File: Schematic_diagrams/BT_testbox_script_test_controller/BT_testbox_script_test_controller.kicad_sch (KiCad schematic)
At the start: 28 parts, among them J10 Conn_01x15_Socket, J3 D Sub Conn_15_Pin Female, J4 Conn_01x07_Socket, J5 Conn_7_Pin, SW4 SW_Push

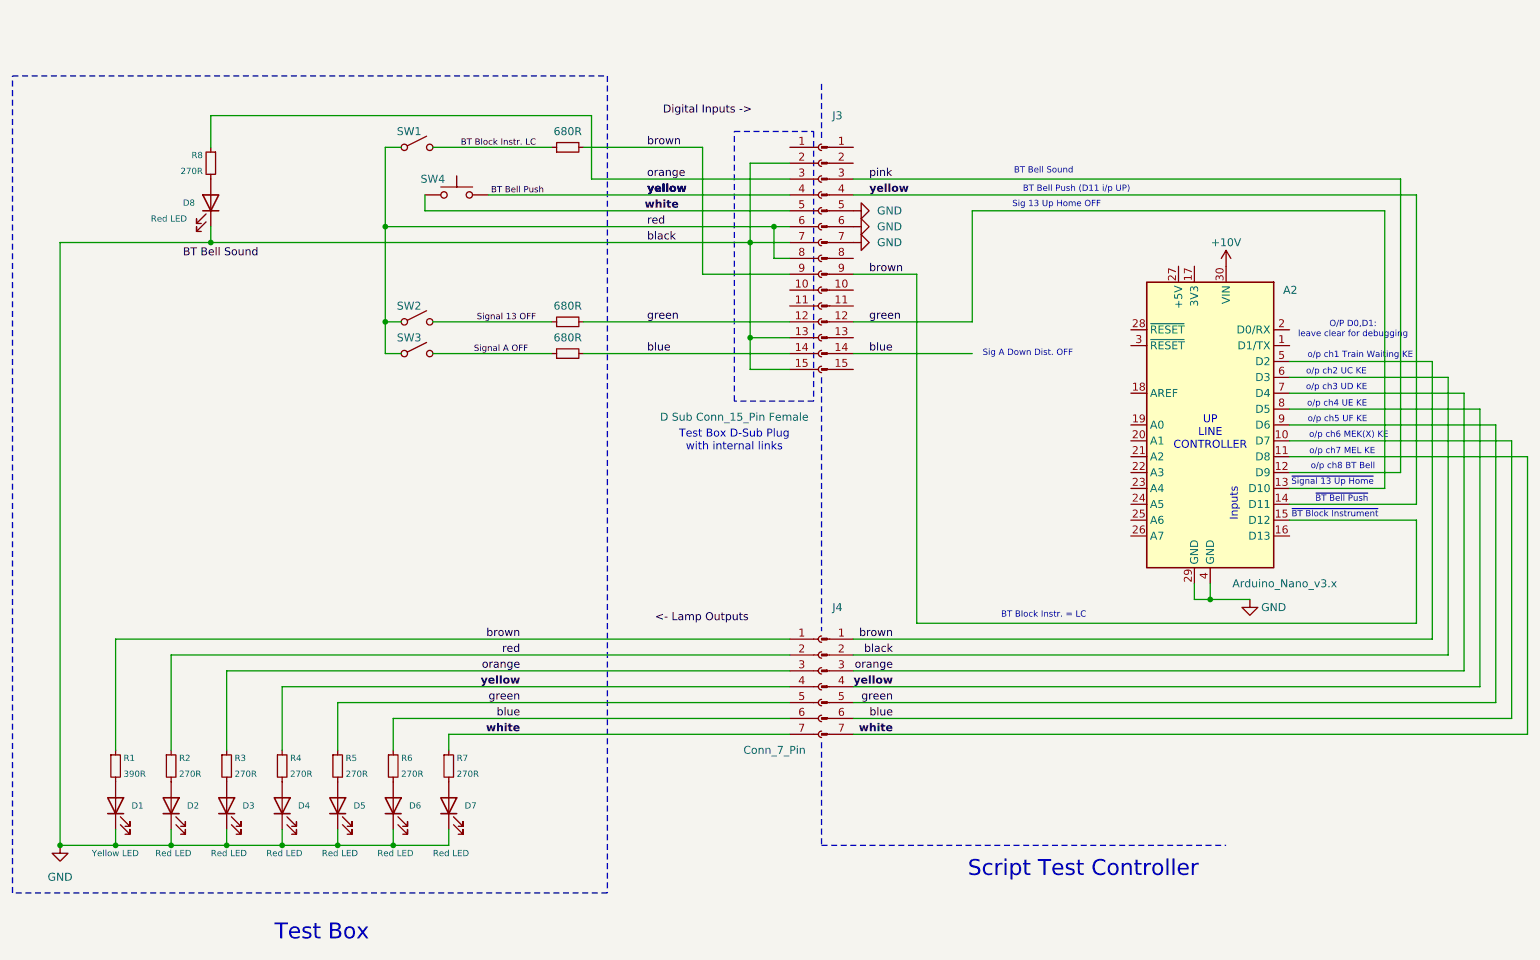
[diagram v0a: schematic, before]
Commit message: internal signal trial
trial was abandoned (inconsistent operation of interrupt)
though some changes were made to wiring and delays
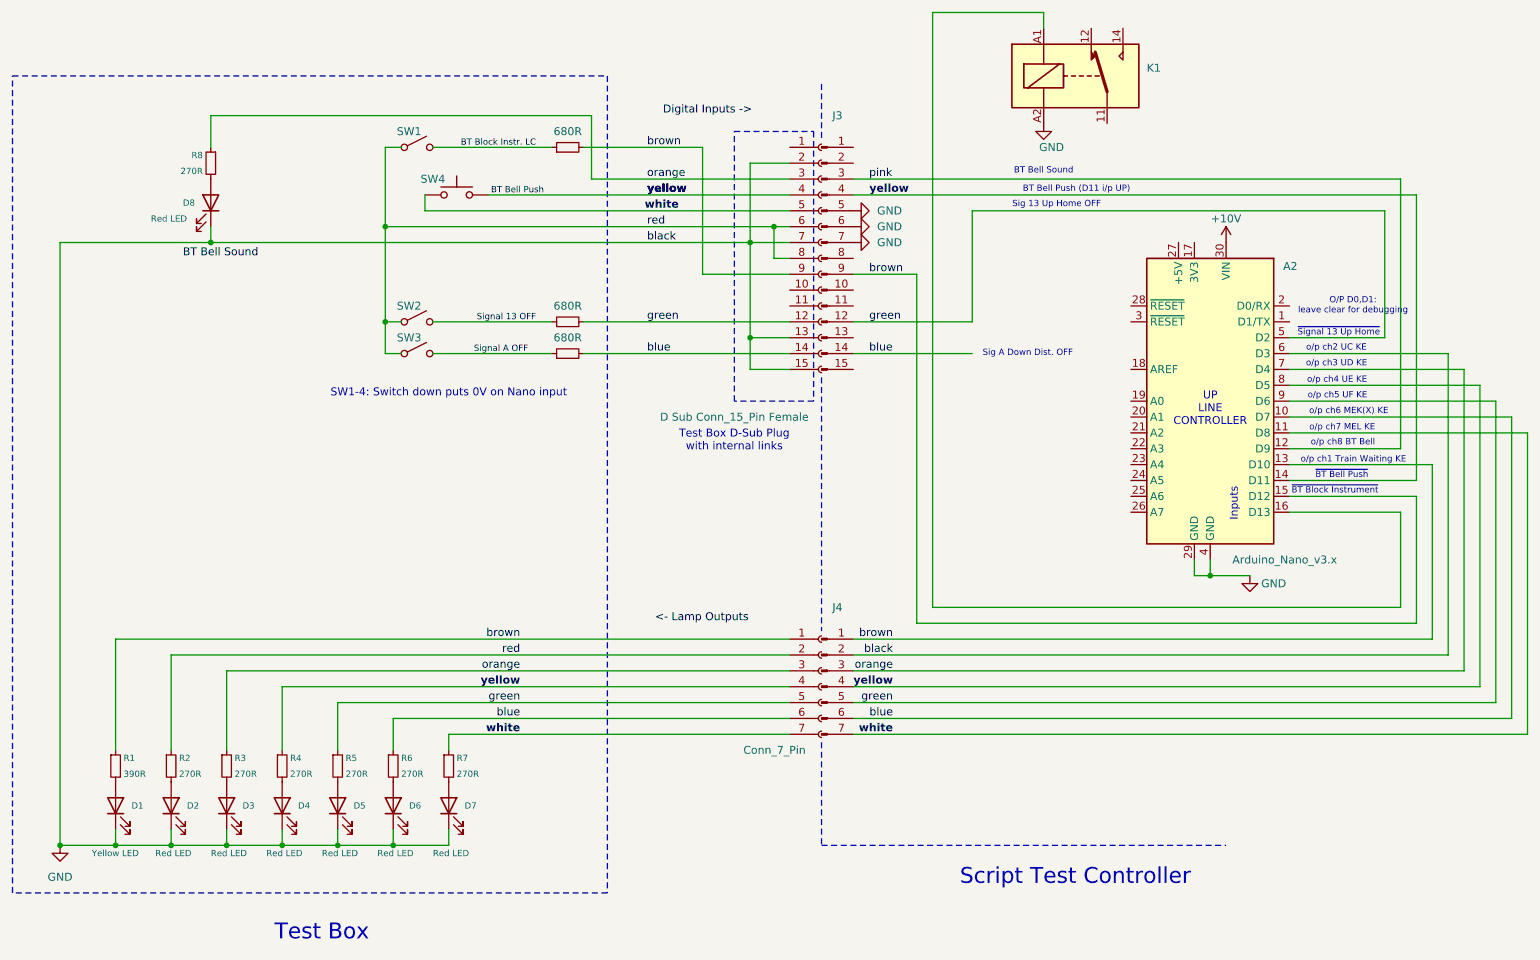
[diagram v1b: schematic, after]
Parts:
- added K1: ~, Relay_THT:Relay_SPDT_Fujitsu_FTR-LYCA005x_FormC_Vertical, symbol Relay:Fujitsu_FTR-LYCA005x
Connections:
- net GND: now also K1.A2
- net brown: now also A2.13 (D10); no longer A2.5 (D2)
- net green: now also A2.5 (D2); no longer A2.13 (D10)
- net at A2.16 (D13): now also K1.A1
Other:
- note added: "SW1-4: Switch down puts 0V on Nano input"
- note removed: "BT Block Instr. = LC"
- moved on the sheet: A2

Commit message: Jim request
train held at second lamp until distant reversed
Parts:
- removed K1: ~, Relay_THT:Relay_SPDT_Fujitsu_FTR-LYCA005x_FormC_Vertical, symbol Relay:Fujitsu_FTR-LYCA005x
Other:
- note added: "Sig A Down Dist. OFF (DOWN line test, connect to D9)"
- note removed: "Sig A Down Dist. OFF"
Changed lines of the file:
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@@
 		(company "Amberley Museum")
 		(comment 1 "B: model signal added")
+		(comment 2 "C: model signal removed; wiring shown for UP line test")
 	)
 	(rectangle
@@
 		)
 	)
-	(text "Sig A Down Dist. OFF"
+	(text "Sig A Down Dist. OFF\n(DOWN line test, connect to D9)"
 		(exclude_from_sim no)
-		(at 200.66 72.39 0)
+		(at 200.66 73.66 0)
 		(effects
 			(font
@@
 	(wire
 		(pts
-			(xy 185.42 17.78) (xy 185.42 113.03)
-		)
-		(stroke
-			(width 0)
-			(type default)
-		)
-	)
-	(wire
-		(pts
 			(xy 162.56 54.61) (xy 156.21 54.61)
 		)
@@
 	(wire
 		(pts
-			(xy 260.35 97.79) (xy 242.57 97.79)
-		)
-		(stroke
-			(width 0)
-			(type default)
-		)
-	)
-	(wire
-		(pts
 			(xy 172.72 133.35) (xy 280.67 133.35)
 		)
@@
 	(wire
 		(pts
-			(xy 203.2 20.32) (xy 203.2 17.78)
-		)
-		(stroke
-			(width 0)
-			(type default)
-		)
-	)
-	(wire
-		(pts
 			(xy 107.95 133.35) (xy 162.56 133.35)
 		)
@@
 	(wire
 		(pts
-			(xy 260.35 113.03) (xy 260.35 97.79)
-		)
-		(stroke
-			(width 0)
-			(type default)
-		)
-	)
-	(wire
-		(pts
 			(xy 156.21 41.91) (xy 156.21 54.61)
 		)
@@
 	(wire
 		(pts
-			(xy 185.42 113.03) (xy 260.35 113.03)
-		)
-		(stroke
-			(width 0)
-			(type default)
-		)
-	)
-	(wire
-		(pts
 			(xy 130.81 34.29) (xy 69.85 34.29)
 		)
@@
 	(wire
 		(pts
-			(xy 203.2 17.78) (xy 185.42 17.78)
-		)
-		(stroke
-			(width 0)
-			(type default)
-		)
-	)
-	(wire
-		(pts
 			(xy 227.33 105.41) (xy 227.33 107.95)
 		)
@@
 	)
 	(symbol
-		(lib_id "power:GND")
-		(at 203.2 35.56 0)
-		(unit 1)
-		(exclude_from_sim no)
-		(in_bom yes)
-		(on_board yes)
-		(dnp no)
-		(property "Reference" "#PWR04"
-			(at 203.2 41.91 0)
-			(effects
-				(font
-					(size 1.27 1.27)
-				)
-				(hide yes)
-			)
-		)
-		(property "Value" "GND"
-			(at 204.47 39.37 0)
-			(effects
-				(font
-					(size 1.27 1.27)
-				)
-			)
-		)
-		(property "Footprint" ""
-			(at 203.2 35.56 0)
-			(effects
-				(font
-					(size 1.27 1.27)
-				)
-				(hide yes)
-			)
-		)
-		(property "Datasheet" ""
-			(at 203.2 35.56 0)
-			(effects
-				(font
-					(size 1.27 1.27)
-				)
-				(hide yes)
-			)
-		)
-		(property "Description" "Power symbol creates a global label with name \"GND\" , ground"
-			(at 203.2 35.56 0)
-			(effects
-				(font
-					(size 1.27 1.27)
-				)
-				(hide yes)
-			)
-		)
-		(pin "1"
-		)
-		(instances
-			(project ""
-				(path "/aad29df0-d981-468f-91fb-fd321cbc3a70"
-					(reference "#PWR04")
-					(unit 1)
-				)
-			)
-		)
-	)
-	(symbol
 		(lib_id "Device:LED")
 		(at 69.85 48.26 270)
@@
 					(unit 1)
 				)
-			)
-		)
-	)
-	(symbol
-		(lib_id "Relay:Fujitsu_FTR-LYCA005x")
-		(at 208.28 27.94 0)
-		(unit 1)
-		(exclude_from_sim no)
-		(in_bom yes)
-		(on_board yes)
-		(dnp no)
-		(fields_autoplaced yes)
-		(property "Reference" "K1"
-			(at 219.71 26.6699 0)
-			(effects
-				(font
-					(size 1.27 1.27)
-				)
-				(justify left)
-			)
-		)
-		(property "Value" "~"
-			(at 219.71 29.2099 0)
-			(effects
-				(font
-					(size 1.27 1.27)
-				)
-				(justify left)
-			)
-		)
-		(property "Footprint" "Relay_THT:Relay_SPDT_Fujitsu_FTR-LYCA005x_FormC_Vertical"
-			(at 219.71 29.21 0)
-			(effects
-				(font
-					(size 1.27 1.27)
-				)
-				(justify left)
-				(hide yes)
-			)
-		)
-		(property "Datasheet" "https://www.fujitsu.com/sg/imagesgig5/ftr-ly.pdf"
-			(at 224.79 31.75 0)
-			(effects
-				(font
-					(size 1.27 1.27)
-				)
-				(justify left)
-				(hide yes)
-			)
-		)
-		(property "Description" "Relay, SPDT Form C, vertical mount, 5-60V coil, 6A, 250VAC, 28 x 5 x 15mm"
-			(at 208.28 27.94 0)
-			(effects
-				(font
-					(size 1.27 1.27)
-				)
-				(hide yes)
-			)
-		)
-		(pin "A1"
-		)
-		(pin "14"
-		)
-		(pin "A2"
-		)
-		(pin "12"
-		)
-		(pin "11"
-		)
-		(instances
-			(project ""
-				(path "/aad29df0-d981-468f-91fb-fd321cbc3a70"
-					(reference "K1")
-					(unit 1)
-				)
